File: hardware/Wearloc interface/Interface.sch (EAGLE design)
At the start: 1 part, among them U1 PCA9306DCT

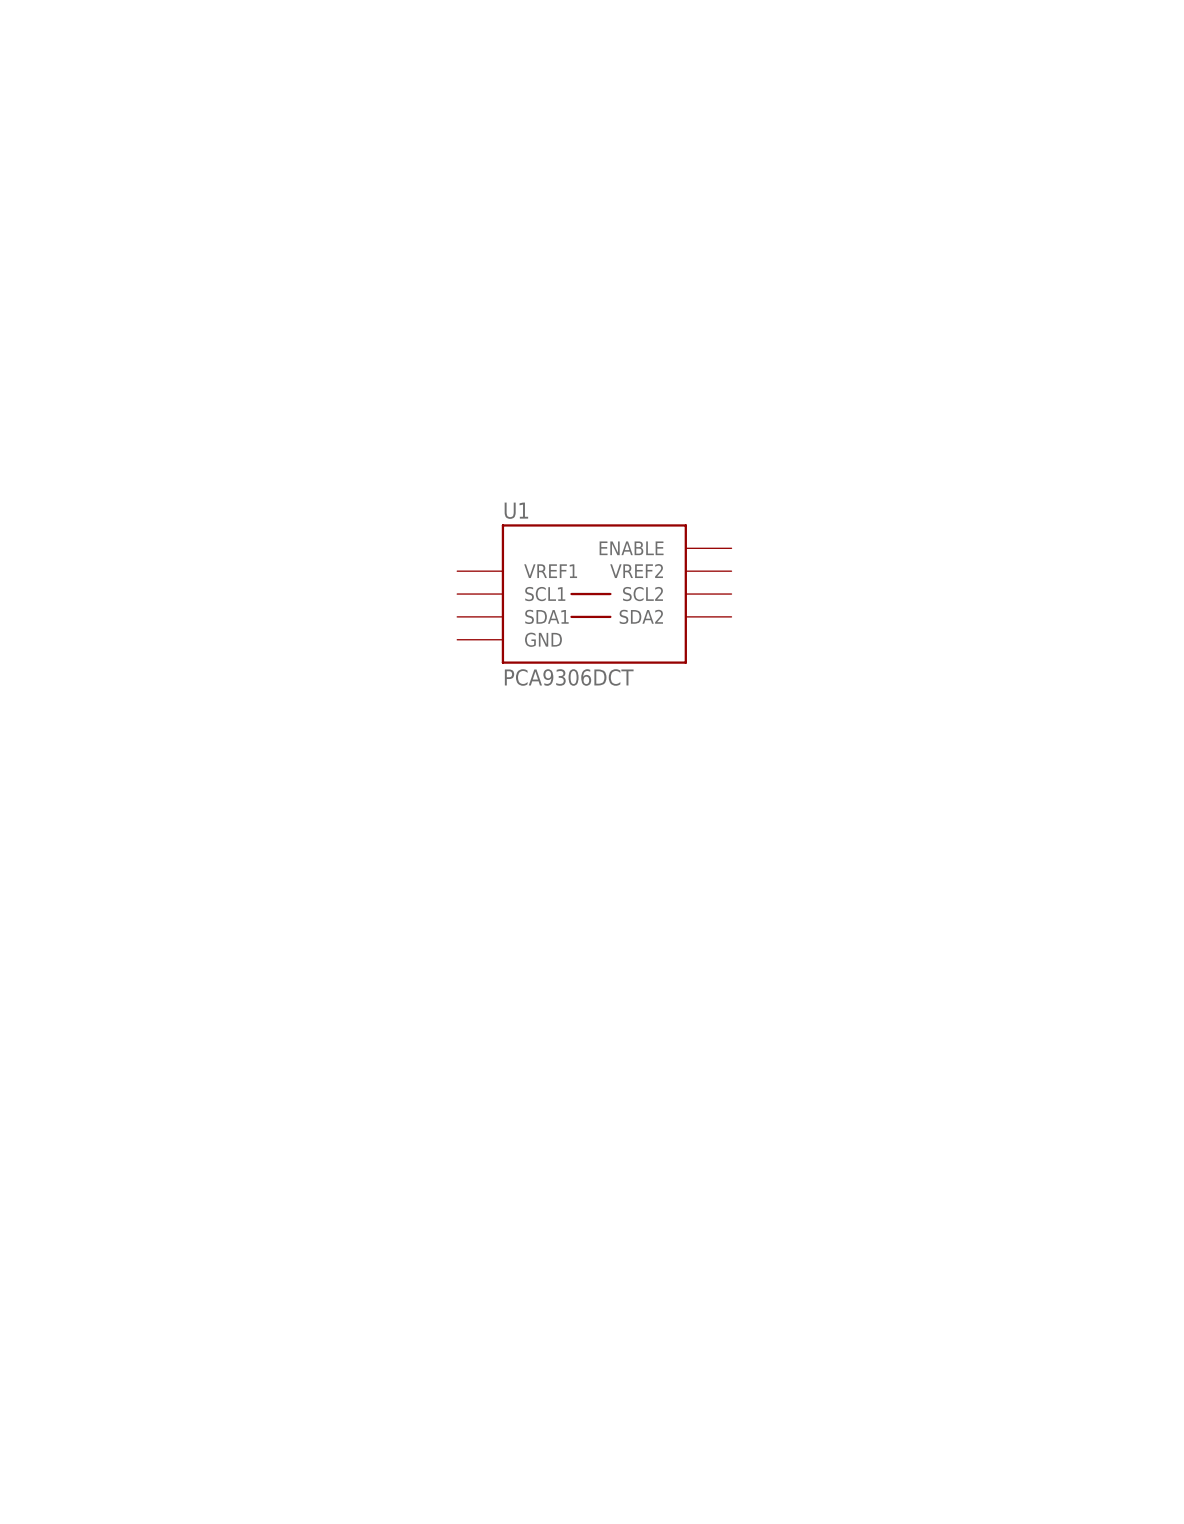
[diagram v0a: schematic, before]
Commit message: started creating interface schematic
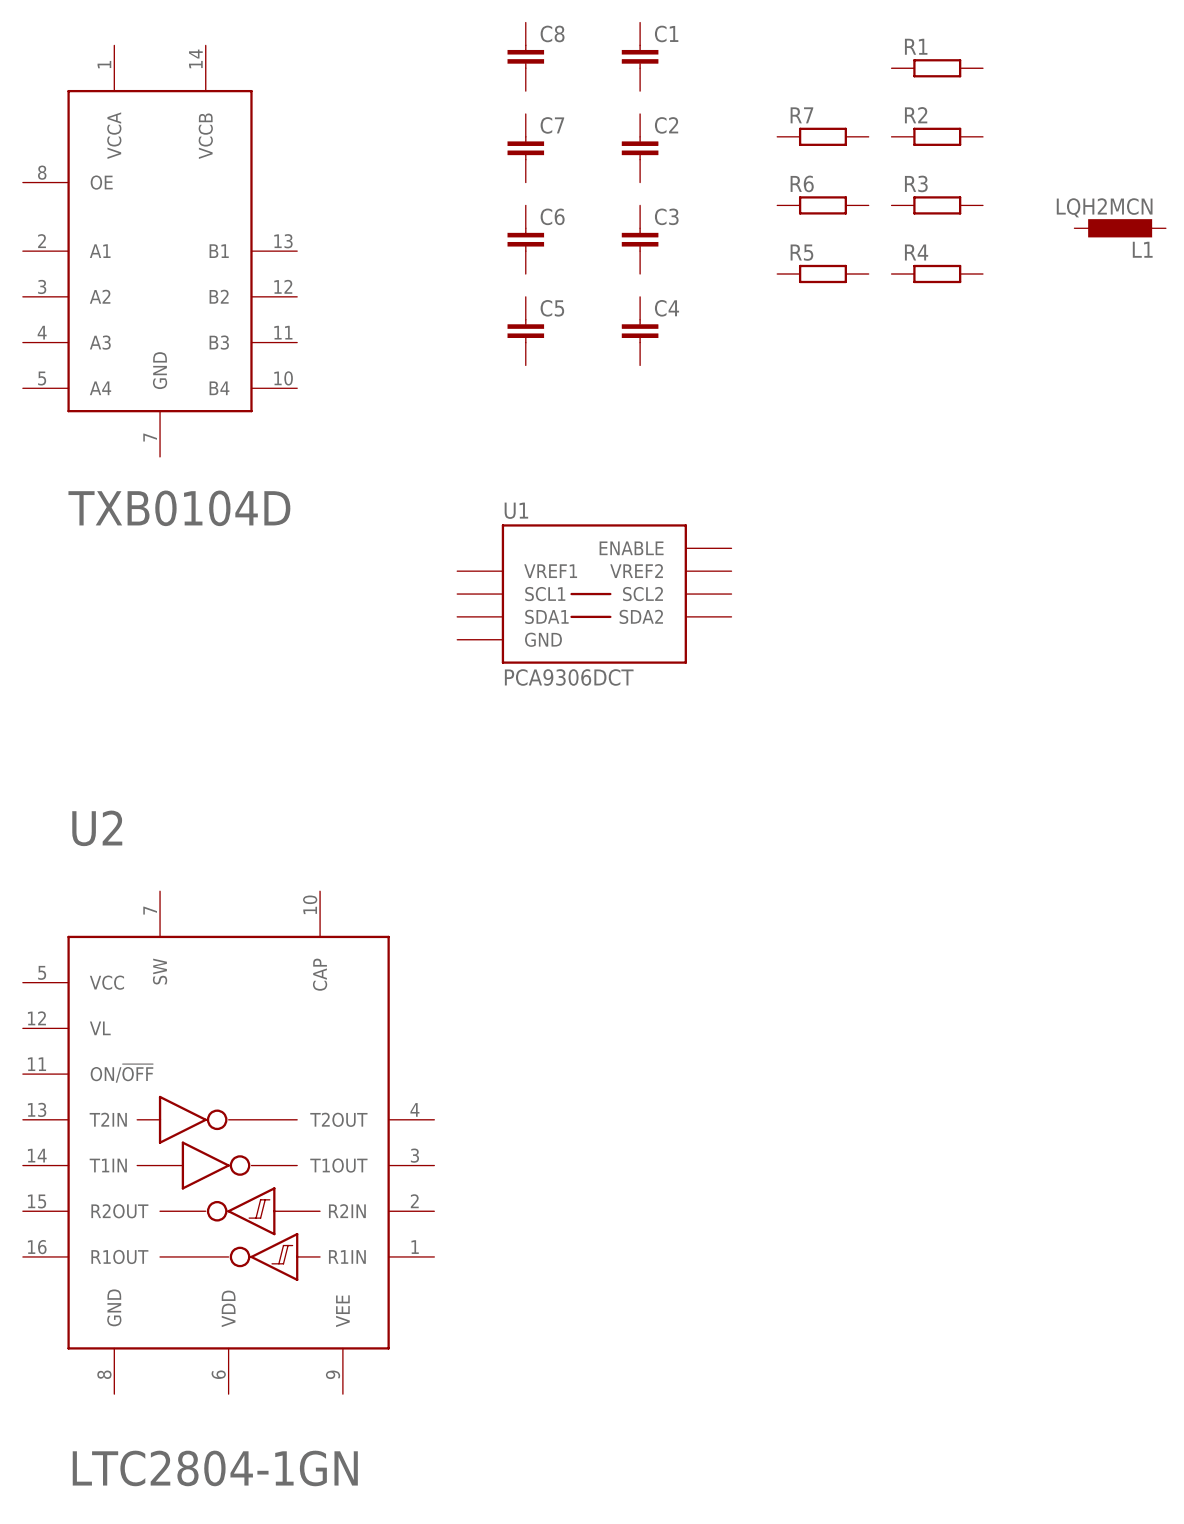
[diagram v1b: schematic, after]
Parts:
- added C1, C2, C3, C4, C5, C6, C7, C8: (no value), rcl:C-EUC0805K
- added L1: LQH2MCN, wearloc:LQH2MCN
- added R1, R2, R3, R4, R5, R6, R7: (no value), rcl:R-EU_R0805
- added U2: LTC2804-1GN, wearloc:LTC2804-1GN
- added U3: TXB0104D, wearloc:TXB0104D
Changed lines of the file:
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@@
 <parts>
 <part name="U1" library="wearloc" deviceset="PCA9306" device="DCT"/>
+<part name="U2" library="wearloc" deviceset="LTC2804-1" device="GN"/>
+<part name="U3" library="wearloc" deviceset="TXB0104" device="D"/>
+<part name="C1" library="rcl" deviceset="C-EU" device="C0805K"/>
+<part name="R1" library="rcl" deviceset="R-EU_" device="R0805"/>
+<part name="L1" library="wearloc" deviceset="LQH2MC" device="N"/>
+<part name="C2" library="rcl" deviceset="C-EU" device="C0805K"/>
+<part name="C3" library="rcl" deviceset="C-EU" device="C0805K"/>
+<part name="C4" library="rcl" deviceset="C-EU" device="C0805K"/>
+<part name="C5" library="rcl" deviceset="C-EU" device="C0805K"/>
+<part name="C6" library="rcl" deviceset="C-EU" device="C0805K"/>
+<part name="C7" library="rcl" deviceset="C-EU" device="C0805K"/>
+<part name="C8" library="rcl" deviceset="C-EU" device="C0805K"/>
+<part name="R2" library="rcl" deviceset="R-EU_" device="R0805"/>
+<part name="R3" library="rcl" deviceset="R-EU_" device="R0805"/>
+<part name="R4" library="rcl" deviceset="R-EU_" device="R0805"/>
+<part name="R5" library="rcl" deviceset="R-EU_" device="R0805"/>
+<part name="R6" library="rcl" deviceset="R-EU_" device="R0805"/>
+<part name="R7" library="rcl" deviceset="R-EU_" device="R0805"/>
 </parts>
 <sheets>
@@
 <instances>
 <instance part="U1" gate="PCA9306" x="25.4" y="15.24"/>
+<instance part="U2" gate="LTC2804-1" x="-15.24" y="-45.72"/>
+<instance part="U3" gate="TXB0104" x="-22.86" y="53.34"/>
+<instance part="C1" gate="G$1" x="30.48" y="76.2"/>
+<instance part="R1" gate="G$1" x="63.5" y="73.66"/>
+<instance part="L1" gate="LQH2MC" x="83.82" y="55.88" rot="R90"/>
+<instance part="C2" gate="G$1" x="30.48" y="66.04"/>
+<instance part="C3" gate="G$1" x="30.48" y="55.88"/>
+<instance part="C4" gate="G$1" x="30.48" y="45.72"/>
+<instance part="C5" gate="G$1" x="17.78" y="45.72"/>
+<instance part="C6" gate="G$1" x="17.78" y="55.88"/>
+<instance part="C7" gate="G$1" x="17.78" y="66.04"/>
+<instance part="C8" gate="G$1" x="17.78" y="76.2"/>
+<instance part="R2" gate="G$1" x="63.5" y="66.04"/>
+<instance part="R3" gate="G$1" x="63.5" y="58.42"/>
+<instance part="R4" gate="G$1" x="63.5" y="50.8"/>
+<instance part="R5" gate="G$1" x="50.8" y="50.8"/>
+<instance part="R6" gate="G$1" x="50.8" y="58.42"/>
+<instance part="R7" gate="G$1" x="50.8" y="66.04"/>
 </instances>
 <busses>

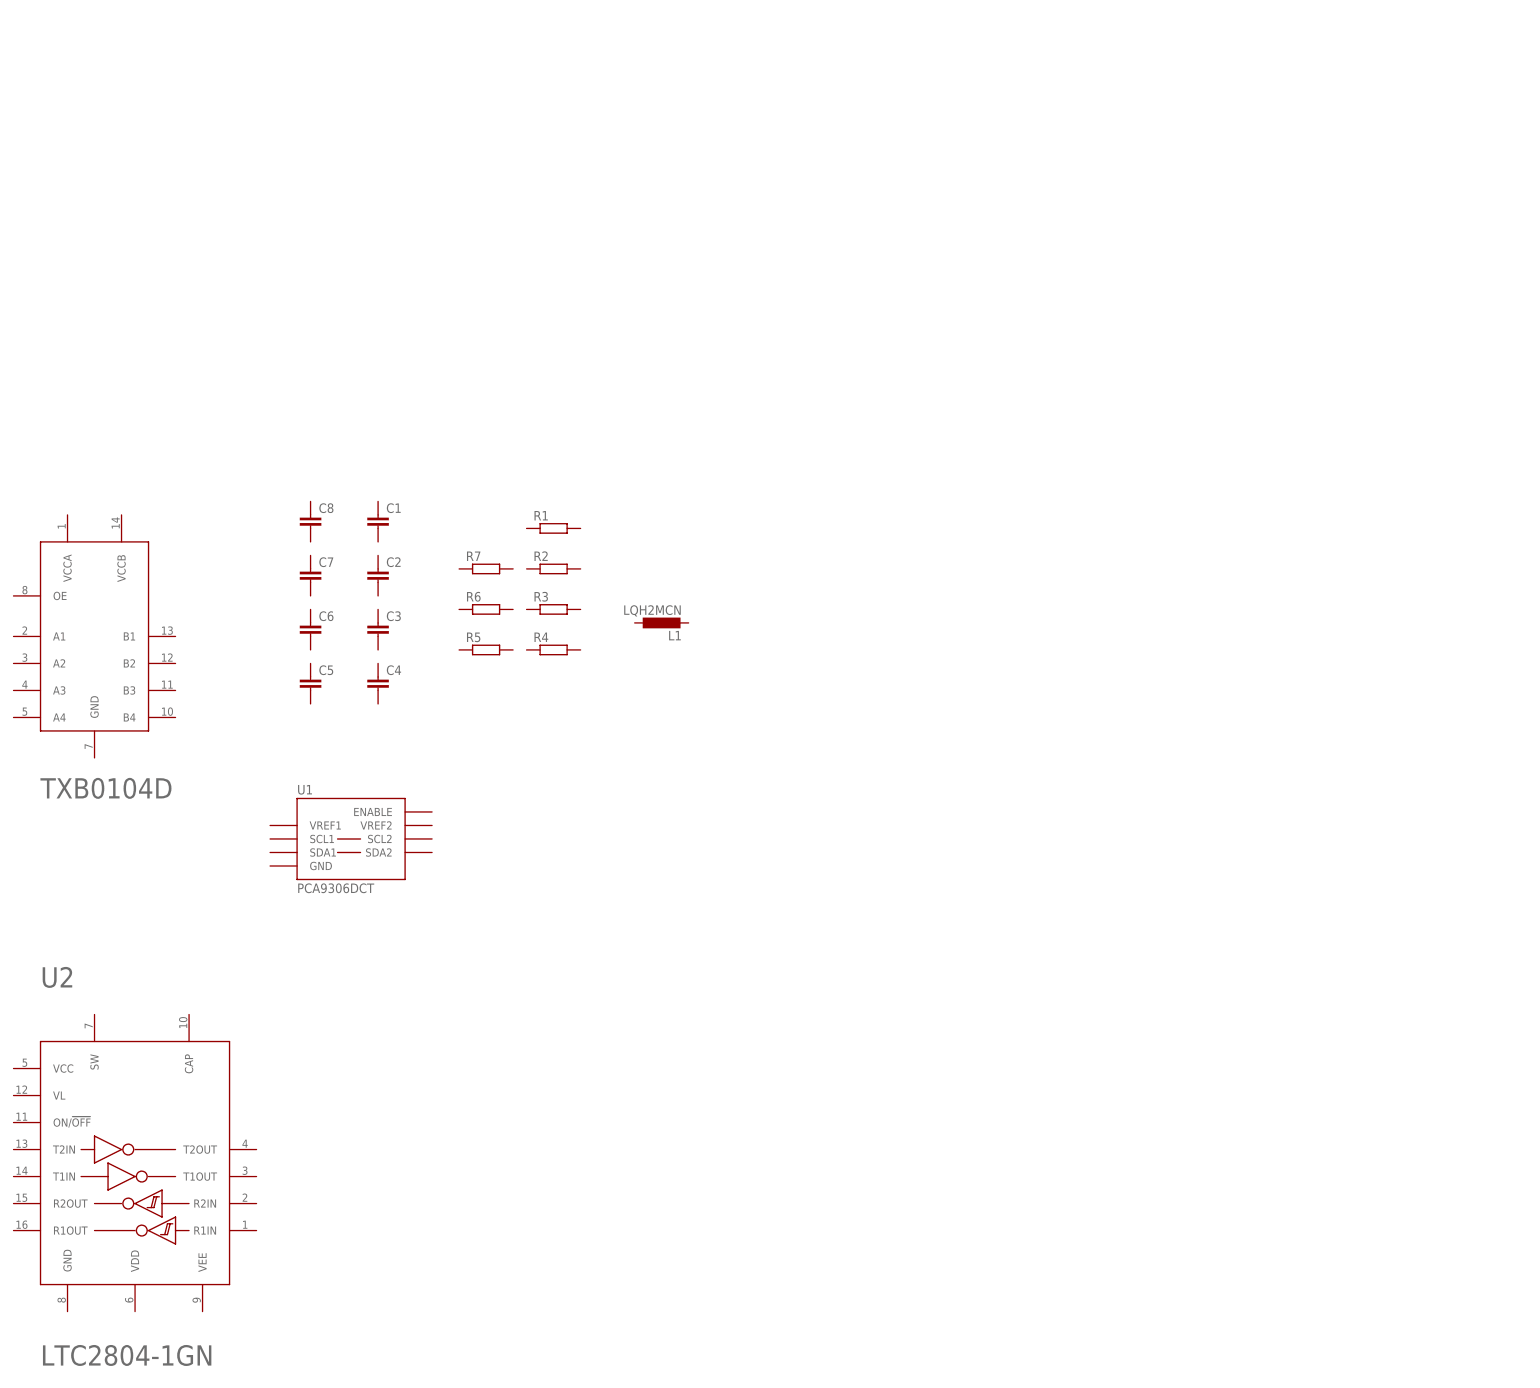
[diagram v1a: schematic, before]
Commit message: Developed interface schematic and its devices.
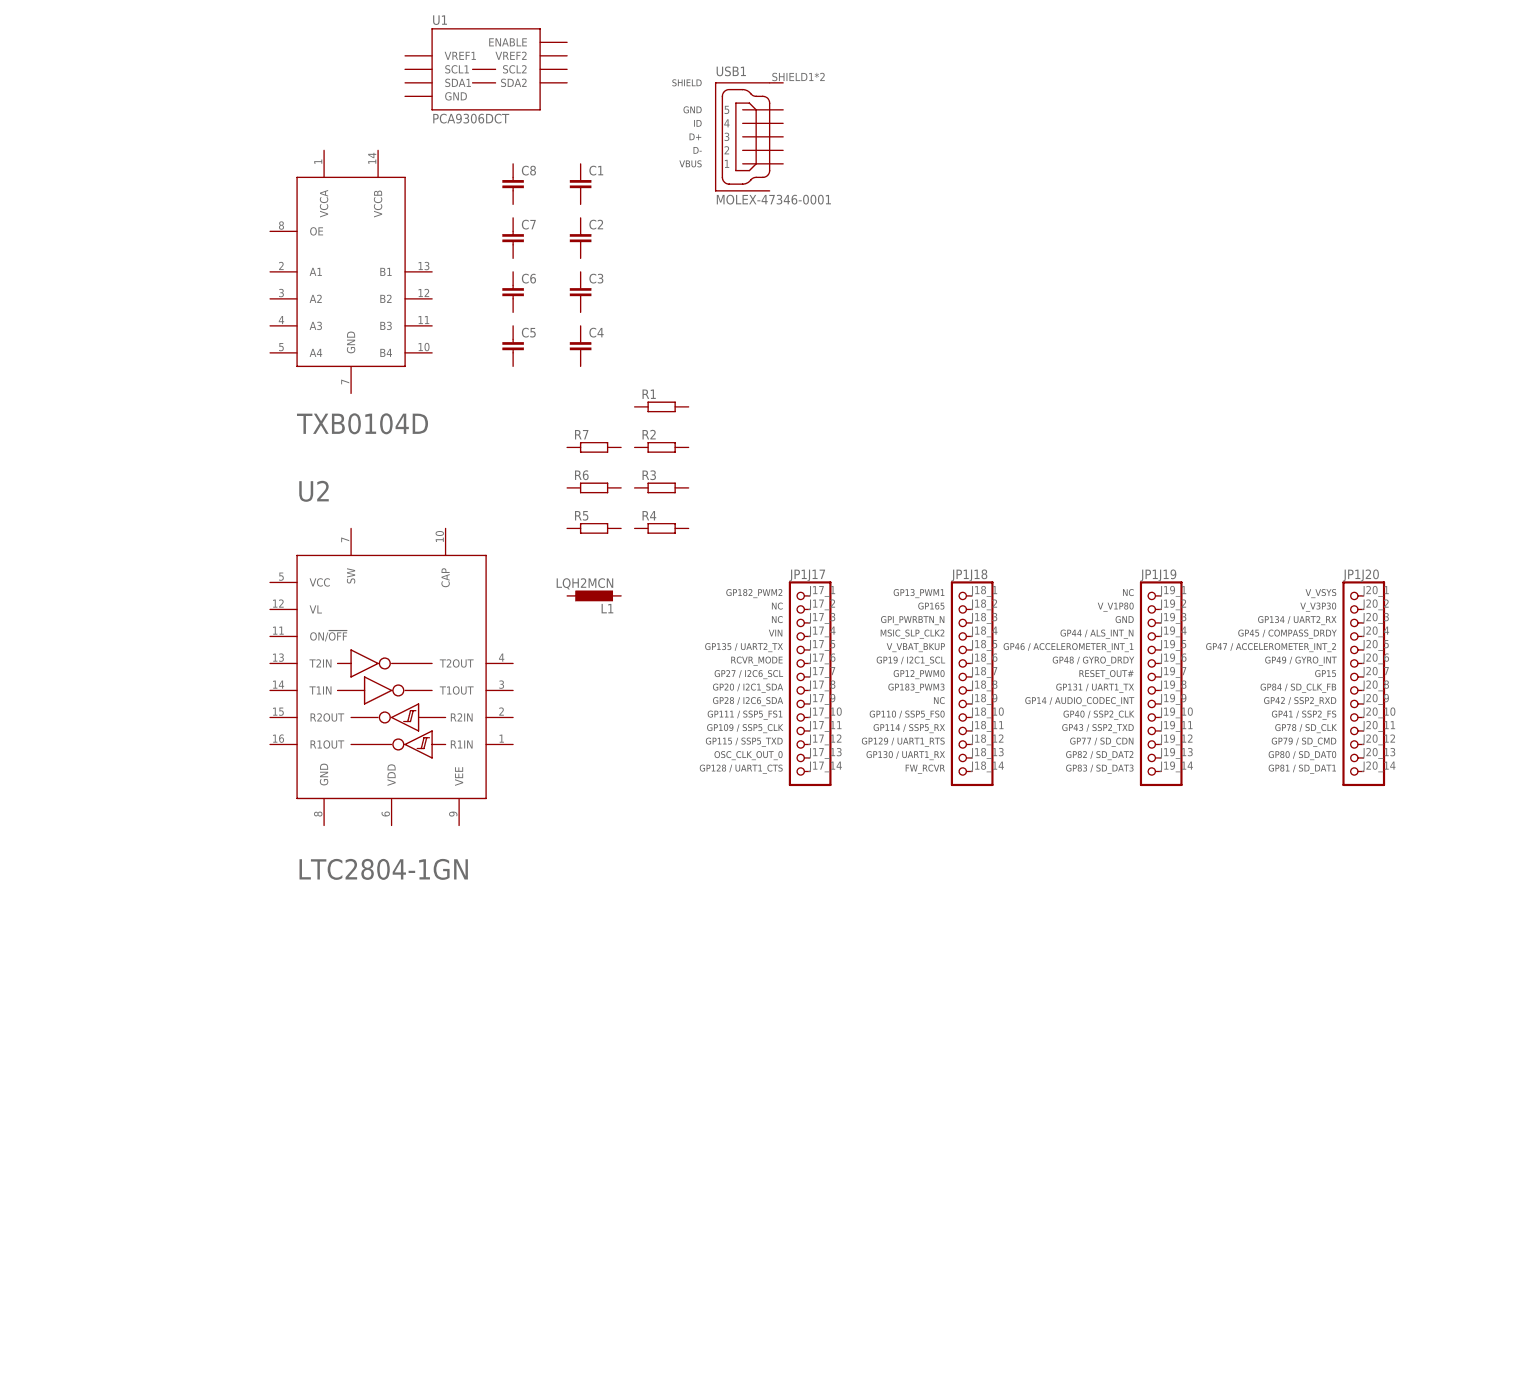
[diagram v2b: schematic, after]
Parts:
- added JP1: (no value), wearloc:INTEL_EDISON_BB_HEADER
- added USB1: MOLEX-47346-0001, wearloc:MOLEX-47346-0001
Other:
- moved on the sheet: C1, C2, C3, C4, C5, C6, C7, C8, L1, R1, R2, R3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
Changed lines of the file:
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@@
 <layer number="112" name="tSilk" color="7" fill="1" visible="yes" active="yes"/>
 <layer number="116" name="Patch_BOT" color="9" fill="4" visible="yes" active="yes"/>
+<layer number="120" name="Descript" color="7" fill="1" visible="yes" active="yes"/>
 <layer number="121" name="_tsilk" color="7" fill="1" visible="yes" active="yes"/>
 <layer number="122" name="_bsilk" color="7" fill="1" visible="yes" active="yes"/>
@@
 <part name="R6" library="rcl" deviceset="R-EU_" device="R0805"/>
 <part name="R7" library="rcl" deviceset="R-EU_" device="R0805"/>
+<part name="JP1" library="wearloc" deviceset="INTEL_EDISON_BB_HEADER" device=""/>
+<part name="FRAME1" library="frames" deviceset="A4L-LOC" device=""/>
+<part name="USB1" library="wearloc" deviceset="MOLEX-47346-0001" device=""/>
 </parts>
 <sheets>
@@
 </plain>
 <instances>
-<instance part="U1" gate="PCA9306" x="25.4" y="15.24"/>
-<instance part="U2" gate="LTC2804-1" x="-15.24" y="-45.72"/>
-<instance part="U3" gate="TXB0104" x="-22.86" y="53.34"/>
-<instance part="C1" gate="G$1" x="30.48" y="76.2"/>
-<instance part="R1" gate="G$1" x="63.5" y="73.66"/>
-<instance part="L1" gate="LQH2MC" x="83.82" y="55.88" rot="R90"/>
-<instance part="C2" gate="G$1" x="30.48" y="66.04"/>
-<instance part="C3" gate="G$1" x="30.48" y="55.88"/>
-<instance part="C4" gate="G$1" x="30.48" y="45.72"/>
-<instance part="C5" gate="G$1" x="17.78" y="45.72"/>
-<instance part="C6" gate="G$1" x="17.78" y="55.88"/>
-<instance part="C7" gate="G$1" x="17.78" y="66.04"/>
-<instance part="C8" gate="G$1" x="17.78" y="76.2"/>
-<instance part="R2" gate="G$1" x="63.5" y="66.04"/>
-<instance part="R3" gate="G$1" x="63.5" y="58.42"/>
-<instance part="R4" gate="G$1" x="63.5" y="50.8"/>
-<instance part="R5" gate="G$1" x="50.8" y="50.8"/>
-<instance part="R6" gate="G$1" x="50.8" y="58.42"/>
-<instance part="R7" gate="G$1" x="50.8" y="66.04"/>
+<instance part="U1" gate="PCA9306" x="50.8" y="160.02"/>
+<instance part="U2" gate="LTC2804-1" x="33.02" y="45.72"/>
+<instance part="U3" gate="TXB0104" x="25.4" y="121.92"/>
+<instance part="C1" gate="G$1" x="68.58" y="139.7"/>
+<instance part="R1" gate="G$1" x="83.82" y="96.52"/>
+<instance part="L1" gate="LQH2MC" x="71.12" y="60.96" rot="R90"/>
+<instance part="C2" gate="G$1" x="68.58" y="129.54"/>
+<instance part="C3" gate="G$1" x="68.58" y="119.38"/>
+<instance part="C4" gate="G$1" x="68.58" y="109.22"/>
+<instance part="C5" gate="G$1" x="55.88" y="109.22"/>
+<instance part="C6" gate="G$1" x="55.88" y="119.38"/>
+<instance part="C7" gate="G$1" x="55.88" y="129.54"/>
+<instance part="C8" gate="G$1" x="55.88" y="139.7"/>
+<instance part="R2" gate="G$1" x="83.82" y="88.9"/>
+<instance part="R3" gate="G$1" x="83.82" y="81.28"/>
+<instance part="R4" gate="G$1" x="83.82" y="73.66"/>
+<instance part="R5" gate="G$1" x="71.12" y="73.66"/>
+<instance part="R6" gate="G$1" x="71.12" y="81.28"/>
+<instance part="R7" gate="G$1" x="71.12" y="88.9"/>
+<instance part="JP1" gate="J17" x="111.76" y="45.72"/>
+<instance part="JP1" gate="J18" x="142.24" y="45.72"/>
+<instance part="JP1" gate="J19" x="177.8" y="45.72"/>
+<instance part="JP1" gate="J20" x="215.9" y="45.72"/>
+<instance part="FRAME1" gate="G$1" x="0" y="0"/>
+<instance part="USB1" gate="MICRO-USB" x="99.06" y="147.32"/>
 </instances>
 <busses>
